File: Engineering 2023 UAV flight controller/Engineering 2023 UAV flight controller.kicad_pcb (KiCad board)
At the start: 2 copper layers, 110 parts, among them IC1 LM2577SX-ADJ_NOPB, J1 Micro_SD_Card, J10 DIO, J2 ESC speed control, J3 USB_C_Receptacle_USB2.0, J4 Conn_Coaxial, J5 external power rail, J6 GPIO, J7 external ground rail, J8 Conn_01x03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

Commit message: more pcb fixing
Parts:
- removed C37, C44: 10u, Capacitor_SMD:C_0603_1608Metric
- removed C8: >1000u, Capacitor_SMD:CP_Elec_5x3
- removed C9: 100u, Capacitor_SMD:C_0603_1608Metric
- removed IC1: LM2577SX-ADJ_NOPB, Package_TO_SOT_SMD:TO-263-5_TabPin3
- added U10: LM2577SX-ADJ_NOPB, Package_TO_SOT_SMD:TO-263-5_TabPin3, F.Cu at (255.6, 109.4)
- moved H4 99.9 mm to (62.8, 43.2)
- moved C14 93.1 mm to (267.3, 67.8)
- moved C27 93.1 mm to (267.3, 65.3)
- moved C3 93.1 mm to (276.5, 60.1)
- moved R20 93.1 mm to (276.5, 62.6)
- moved U6 93.1 mm to (267.4, 60.9)
- moved FB1 93.1 mm to (206.8, 79.3)
- moved FB2 93.1 mm to (206.8, 81.3)
- moved J10 93.1 mm to (211.3, 99.7)
- moved J5 93.1 mm to (206.3, 53.1)
- moved SW2 93.1 mm to (203.5, 96.6)
- moved U2 93.1 mm to (192.0, 98.0)
- moved C1 93.1 mm to (215.6, 98.6)
- moved C10 93.1 mm to (234.0, 98.7)
- moved C11 93.1 mm to (253.3, 81.6)
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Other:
- board outline added: 96.9 x 100 mm

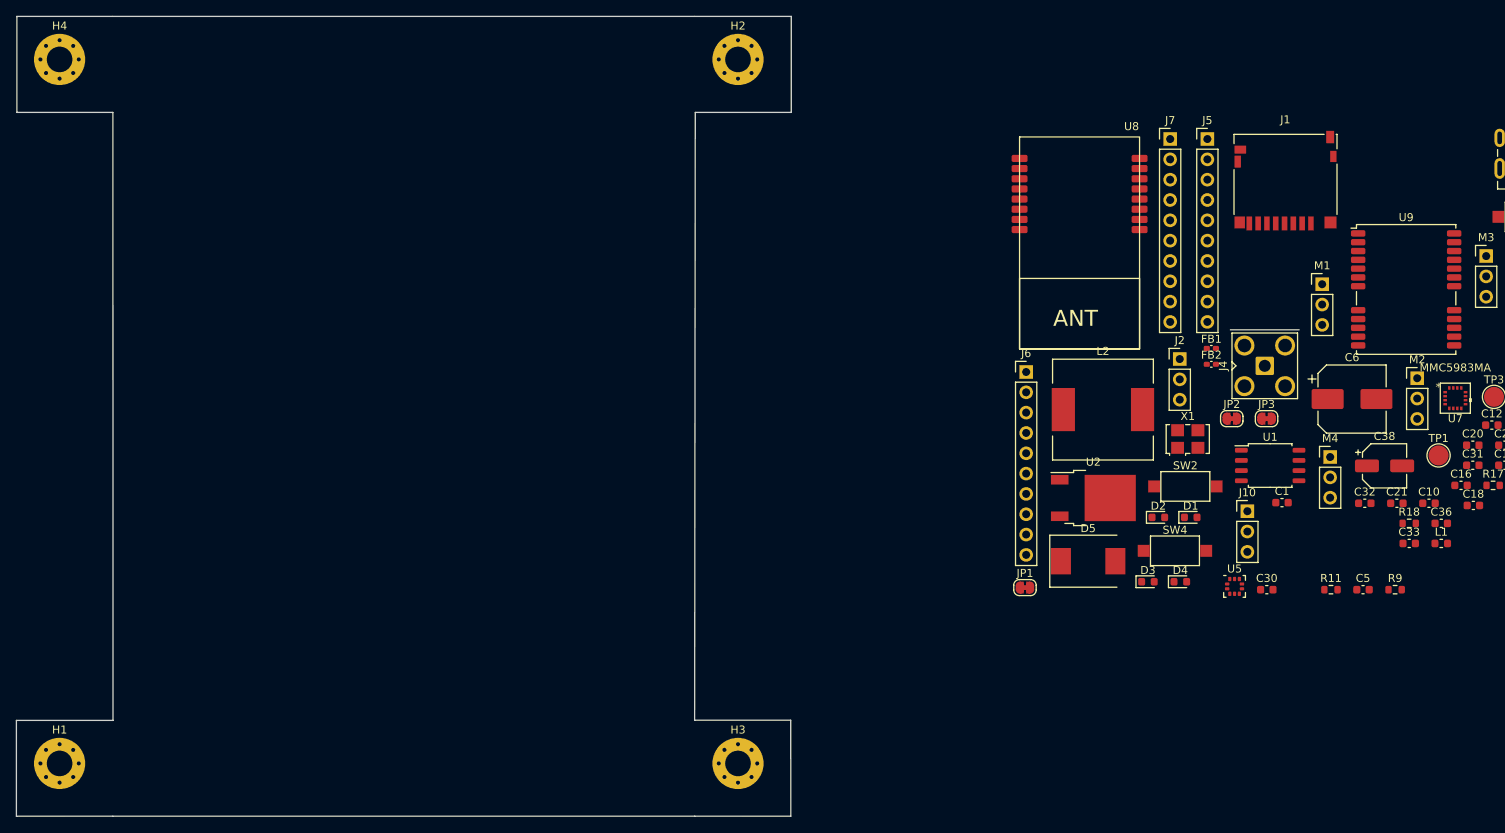
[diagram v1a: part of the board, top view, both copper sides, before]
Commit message: started pcb layout mk2
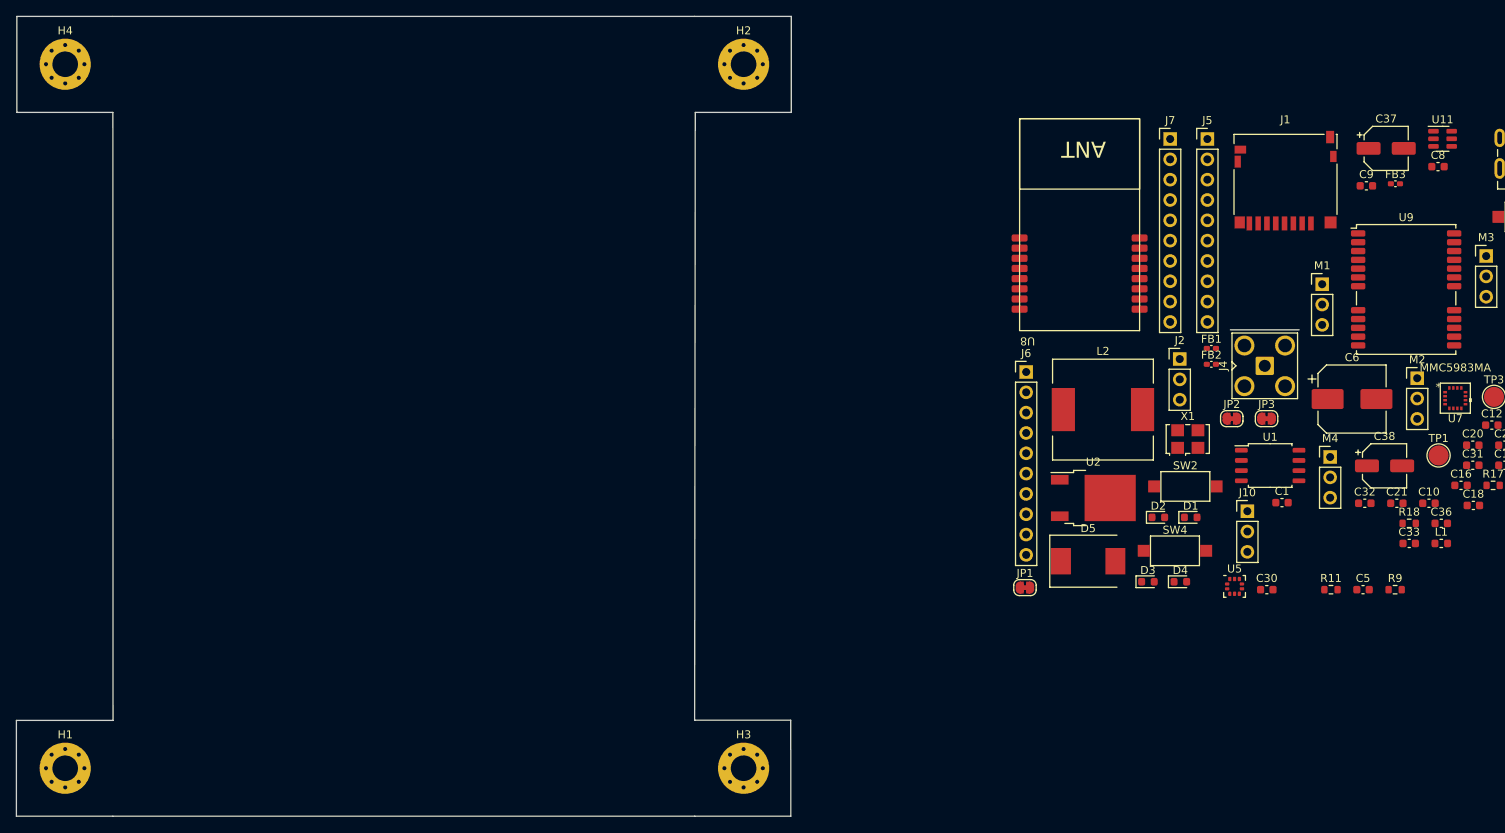
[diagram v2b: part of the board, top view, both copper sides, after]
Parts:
- added C37: 4u7, Capacitor_SMD:CP_Elec_5x3, F.Cu at (228.6, 54.3)
- added C8: 10n, Capacitor_SMD:C_0603_1608Metric, F.Cu at (235.1, 56.6)
- added C9: 10n, Capacitor_SMD:C_0603_1608Metric, F.Cu at (226.2, 59.0)
- added FB3: BLM15PX331BH1D, Inductor_SMD:L_0402_1005Metric_Pad0.77x0.64mm_HandSolder, F.Cu at (229.8, 58.7)
- added U11: USBLC6-2SC6, Package_TO_SOT_SMD:SOT-23-6, F.Cu at (235.7, 53.1)
- moved U8 26.9 mm to (190.8, 78.4), turned to 180 degrees
- moved H3 0.92 mm to (148.3, 131.8)
- moved H1 0.92 mm to (63.5, 131.8)
- moved H2 0.92 mm to (148.3, 43.8)
- moved H4 0.92 mm to (63.5, 43.8)
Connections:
- R8 pad 1: /USB_D_P -> /USB_+
- R9 pad 1: /USB_D_N -> /USB_-
- SW1 pad 2: /reg in -> /pwr_in

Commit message: arranged sub units for routing pls dont eat my pcb github
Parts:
- R2: value 4k7 -> 10k
- R20: value 1000 -> 1k8
- moved C25 295.7 mm to (59.2, 267.0)
- moved R12 294.4 mm to (81.0, 267.2)
- moved SW3 289.3 mm to (37.1, 262.4)
- moved U6 286.4 mm to (60.4, 258.8)
- moved C27 286.2 mm to (64.4, 267.2)
- moved C24 274.1 mm to (69.8, 266.6)
- moved J5 273.4 mm to (476.0, 97.8)
- moved J7 267.3 mm to (465.0, 99.0)
- moved R13 263.4 mm to (76.6, 267.2)
- moved J6 263.3 mm to (446.4, 99.6)
- moved C31 261.9 mm to (33.9, 256.2)
- moved U8 258.7 mm to (22.6, 275.0)
- moved M1 257.9 mm to (478.2, 84.5)
- moved C28 257.5 mm to (132.0, 259.4)
- moved R15 253.1 mm to (75.2, 250.2)
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
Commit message: Q
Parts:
- moved C6 54.1 mm to (29.0, 152.2), turned to -90 degrees
- moved TP1 39.3 mm to (29.0, 144.7)
- moved R11 34.4 mm to (22.0, 154.7), turned to -90 degrees
- moved R20 30.5 mm to (44.4, 155.4), turned to 180 degrees
- moved D3 27.8 mm to (22.0, 150.1), turned to 90 degrees
- moved C5 26.5 mm to (46.2, 170.2), turned to -90 degrees
- moved C2 25.8 mm to (35.2, 162.1), turned to 180 degrees
- moved U10 24.2 mm to (39.2, 171.7), turned to -90 degrees
- moved R1 23.4 mm to (46.2, 166.7), turned to -90 degrees
- moved D5 16.5 mm to (37.2, 155.8), turned to -90 degrees
- moved R2 13.6 mm to (44.4, 152.4)
- moved L2 12.7 mm to (26.8, 164.6), turned to 90 degrees
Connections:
- net Net-(C5-Pad1) renamed /R1-C5
- net Net-(D3-Pad1) renamed /LED_SW
- net Net-(R1-Pad1) renamed /COMP
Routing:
- net /Servo 6V rail: track 0.00 -> 27.5 mm
- net GND: track 0.00 -> 22.9 mm, vias 0 -> 15
- net /FEEDBACK: track 0.00 -> 16.8 mm
- net /COMP: track 0.00 -> 3.63 mm
- net /LED_SW: track 0.00 -> 2.99 mm
- net /R1-C5: track 0.00 -> 2.00 mm
- added copper zone on F.Cu, net /L-D
- added copper zone on F.Cu, net /reg in

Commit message: routed some stuff, E
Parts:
- moved M1 439.7 mm to (39.0, 64.4), turned to -90 degrees
- moved M2 434.6 mm to (39.0, 68.2), turned to -90 degrees
- moved M3 428.0 mm to (39.0, 72.0), turned to -90 degrees
- moved M4 420.3 mm to (39.0, 75.8), turned to -90 degrees
- moved J10 413.0 mm to (51.1, 19.3), turned to 90 degrees
- moved J2 352.3 mm to (97.1, 88.0), turned to 90 degrees
- moved J4 249.8 mm to (78.7, 21.9)
- moved U8 246.8 mm to (60.3, 31.1), turned to -90 degrees
- moved L1 244.9 mm to (78.7, 28.1), turned to 90 degrees
- moved SW3 244.1 mm to (63.3, 19.7)
- moved C35 239.5 mm to (76.3, 28.9), turned to 180 degrees
- moved U9 232.7 mm to (95.0, 30.2), turned to 180 degrees
- moved R17 231.9 mm to (81.3, 28.9), turned to 180 degrees
- moved C29 227.7 mm to (86.4, 37.1), turned to -90 degrees
- moved FB2 227.6 mm to (91.8, 42.9), turned to 90 degrees
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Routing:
- net GND: track 22.9 -> 82.5 mm, vias 15 -> 42
- net /USB_C positive rail: track 0.00 -> 45.2 mm, vias 0 -> 2
- net /3.3v rail: track 0.00 -> 35.4 mm, vias 0 -> 1
- net /NEO 3.3v rail: track 0.00 -> 31.3 mm
- net /reg in: track 0.00 -> 30.3 mm, vias 0 -> 9
- net /NEO_RF_IN: track 0.00 -> 28.7 mm
- net /Servo 6V rail: track 27.5 -> 51.3 mm
- net /NEO_VCC_RF: track 0.00 -> 19.9 mm
- net /LORA_~{RESET}: track 0.00 -> 17.7 mm
- net /pwr_in: track 0.00 -> 14.0 mm
- net /NEO_FB_TXD: track 0.00 -> 12.8 mm
- net /NEO_FB_RXD: track 0.00 -> 10.5 mm
- net /NEO_TIMEPULSE: track 0.00 -> 7.54 mm
- net /ESC positive rail: track 0.00 -> 6.65 mm
- net /DIO1: track 0.00 -> 5.39 mm
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- added copper zone on In2.Cu, net /reg in
- added copper zone on In1.Cu, net GND
- added copper zone on In2.Cu, net GND
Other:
- copper layers 2 -> 4

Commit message: 3
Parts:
- moved J5 443.6 mm to (35.9, 42.4)
- moved J7 435.4 mm to (33.3, 42.4)
- moved J6 412.0 mm to (38.4, 42.4)
- moved C38 389.7 mm to (49.1, 83.5)
- moved C19 320.4 mm to (65.6, 65.7), turned to 180 degrees
- moved C17 319.0 mm to (64.2, 59.9), turned to 180 degrees
- moved C14 315.6 mm to (67.8, 68.0), turned to -90 degrees
- moved C18 314.6 mm to (65.6, 64.2), turned to 180 degrees
- moved J8 312.8 mm to (153.5, 32.0)
- moved C12 310.3 mm to (69.3, 68.0), turned to -90 degrees
- moved C15 309.7 mm to (80.1, 59.9)
- moved C11 309.6 mm to (70.1, 53.4), turned to 90 degrees
- moved C16 309.2 mm to (71.7, 53.4), turned to 90 degrees
- moved R8 306.2 mm to (71.5, 72.7), turned to 90 degrees
- moved C20 305.7 mm to (72.1, 68.0), turned to -90 degrees
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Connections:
- U11 pad 1: /USB_D_N -> /USB_D_P
- U11 pad 3: /USB_- -> /USB_+
- U11 pad 4: /USB_+ -> /USB_-
- U11 pad 6: /USB_D_P -> /USB_D_N
- U4 pad 21: /XOUT -> GND
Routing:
- net /3.3v rail: track 35.4 -> 81.2 mm, vias 1 -> 12
- net GND: track 82.5 -> 111.7 mm, vias 42 -> 58
- net /1.1V internal rp2040 reg: track 0.00 -> 19.6 mm, vias 0 -> 6
- net /Servo 6V rail: track 51.3 -> 49.8 mm
- net /LED_SW: track 2.99 -> 1.69 mm
- added copper zone on F.Cu, net /1.1V internal rp2040 reg
- added copper zone on F.Cu, net /3.3v rail
- added copper zone on In2.Cu, net /3.3v rail

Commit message: EE
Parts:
- removed JP1: SolderJumper_2_Bridged, Jumper:SolderJumper-2_P1.3mm_Bridged_RoundedPad1.0x1.5mm
- JP2, JP3: moved to B.Cu
- moved C25 222.4 mm to (78.9, 45.5), turned to 180 degrees
- moved C24 217.3 mm to (75.2, 49.4), turned to 90 degrees
- moved C27 214.6 mm to (76.8, 53.0)
- moved R14 213.9 mm to (88.3, 43.1), turned to 90 degrees
- moved C22 212.4 mm to (73.7, 49.4), turned to 90 degrees
- moved U7 210.7 mm to (84.8, 48.6), turned to -90 degrees
- moved U6 210.2 mm to (78.8, 49.4), turned to 180 degrees
- moved R13 207.7 mm to (82.8, 59.6), turned to -90 degrees
- moved R12 207.6 mm to (84.4, 59.6), turned to -90 degrees
- moved R15 207.3 mm to (86.2, 43.2), turned to -90 degrees
- moved C36 205.5 mm to (83.2, 45.9)
- moved C34 204.5 mm to (88.5, 48.5), turned to -90 degrees
- moved C33 199.5 mm to (85.3, 51.5), turned to 180 degrees
- moved C21 180.8 mm to (84.8, 53.4), turned to 180 degrees
- moved U5 175.8 mm to (84.8, 55.8)
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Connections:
- U5 pad 1: /~{CS} -> /3.3v rail
- U5 pad 6: /~{CS} -> /3.3v rail
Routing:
- net /3.3v rail: track 81.2 -> 82.4 mm, vias 12 -> 13
- net GND: track 111.7 -> 111.5 mm, vias 58 -> 61
